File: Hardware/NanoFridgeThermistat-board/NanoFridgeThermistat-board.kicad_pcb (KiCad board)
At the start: 2 copper layers, 80.5 x 72 mm, 36 parts, among them J1 Connector_Thermistor, J2 Main_Connector, J3 CompressorMotor_Connector, J4 I2C_Conn, SW1 SW_Push, SW2 SW_Push, T1 CST1, U1 MOC3042M, U2 TL072

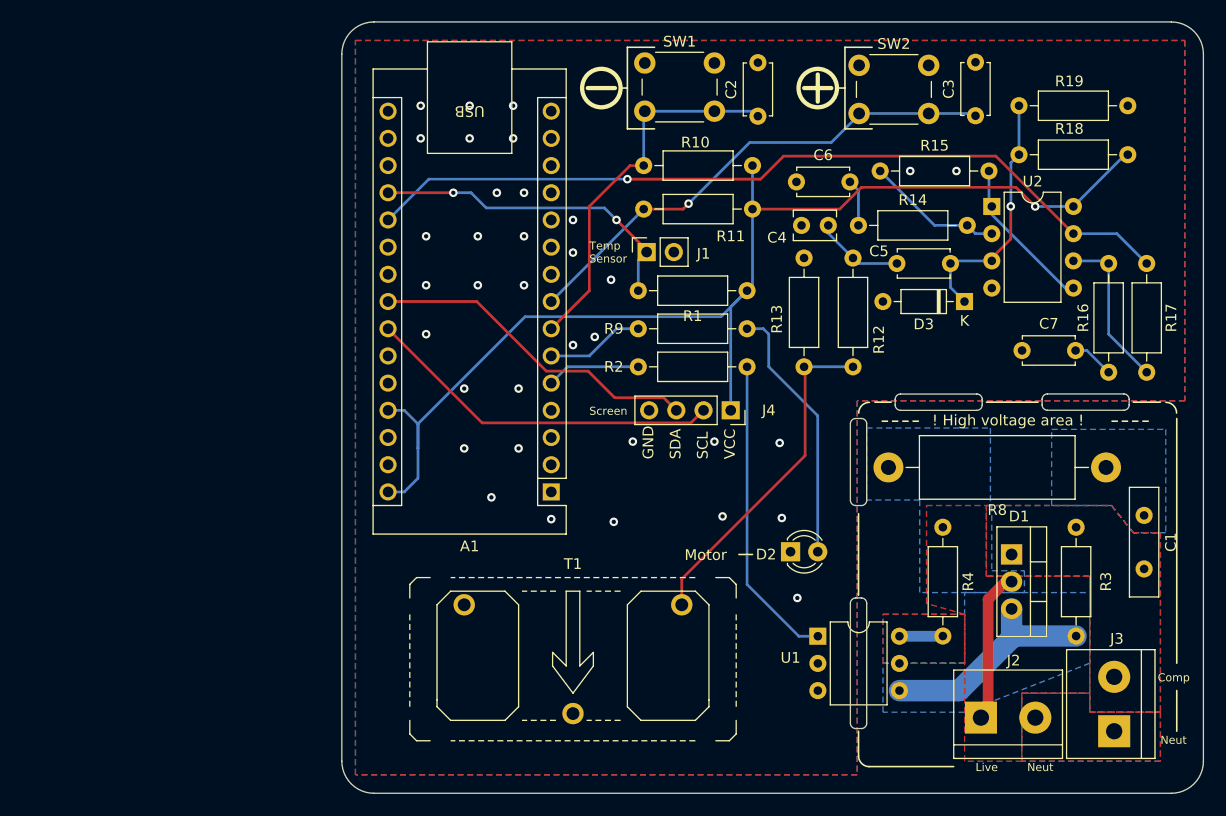
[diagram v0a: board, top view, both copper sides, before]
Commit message: Fixed last issues with DRC on PCB router
Signed-off-by: bebenlebricolo <benoittarrade@hotmail.fr>
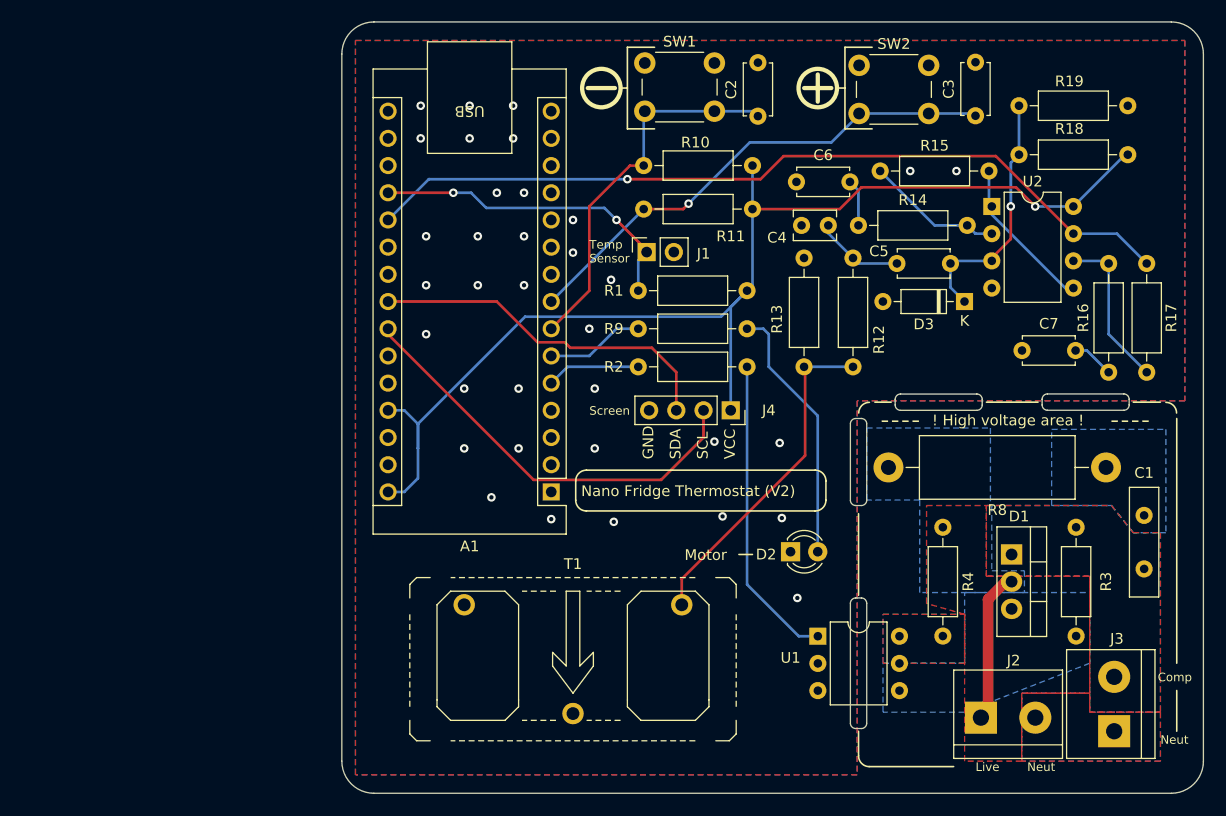
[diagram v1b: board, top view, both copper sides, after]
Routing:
- net /Trigger: track 21.3 -> 0.00 mm
- net SCL: track 33.6 -> 39.8 mm
- net /TriacDriverAC1: track 4.06 -> 0.00 mm
- net SDA: track 31.1 -> 33.2 mm
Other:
- board text added: "Designed by bebenlebricolo (Benoît Tarrade) 05/02/2024 (dd/mm/yyyy) https://github.com/bebenlebricolo/NanoFridgeThermostat"
- board text added: "Licensed under CERN OHL V2"
- board text added: "Nano Fridge Thermostat (V2)"

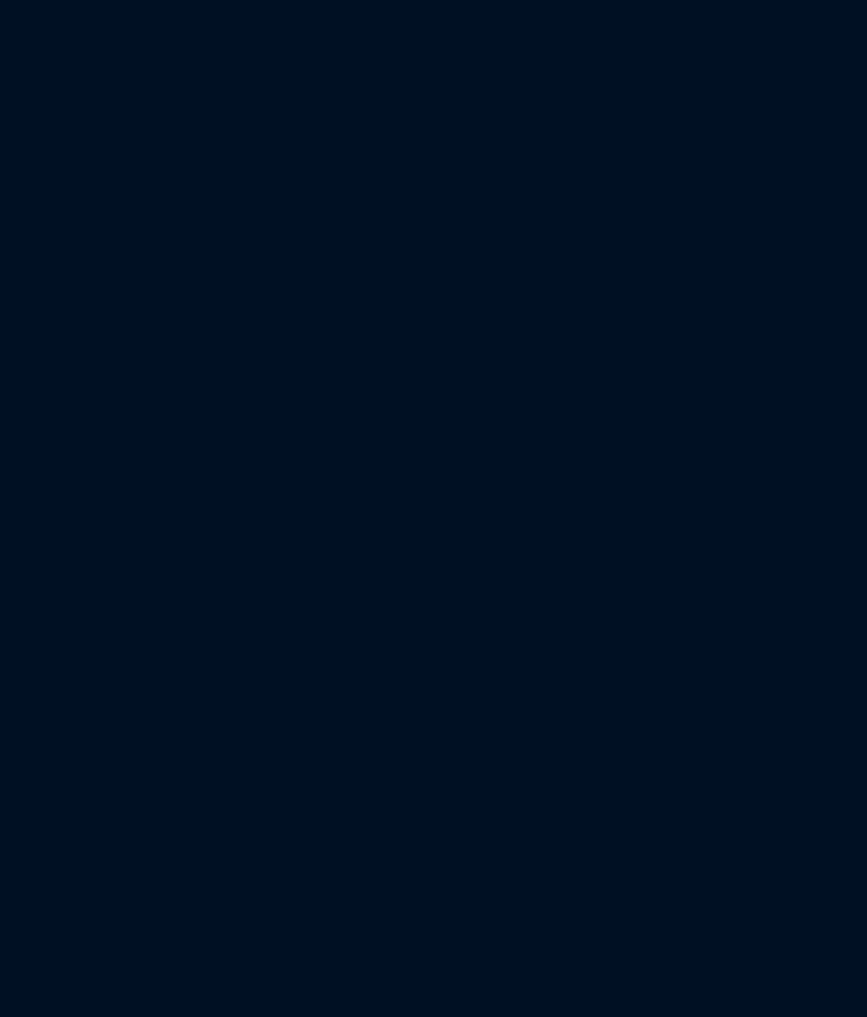
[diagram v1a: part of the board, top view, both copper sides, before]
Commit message: Adding mounting holes and test points
Signed-off-by: bebenlebricolo <benoittarrade@hotmail.fr>
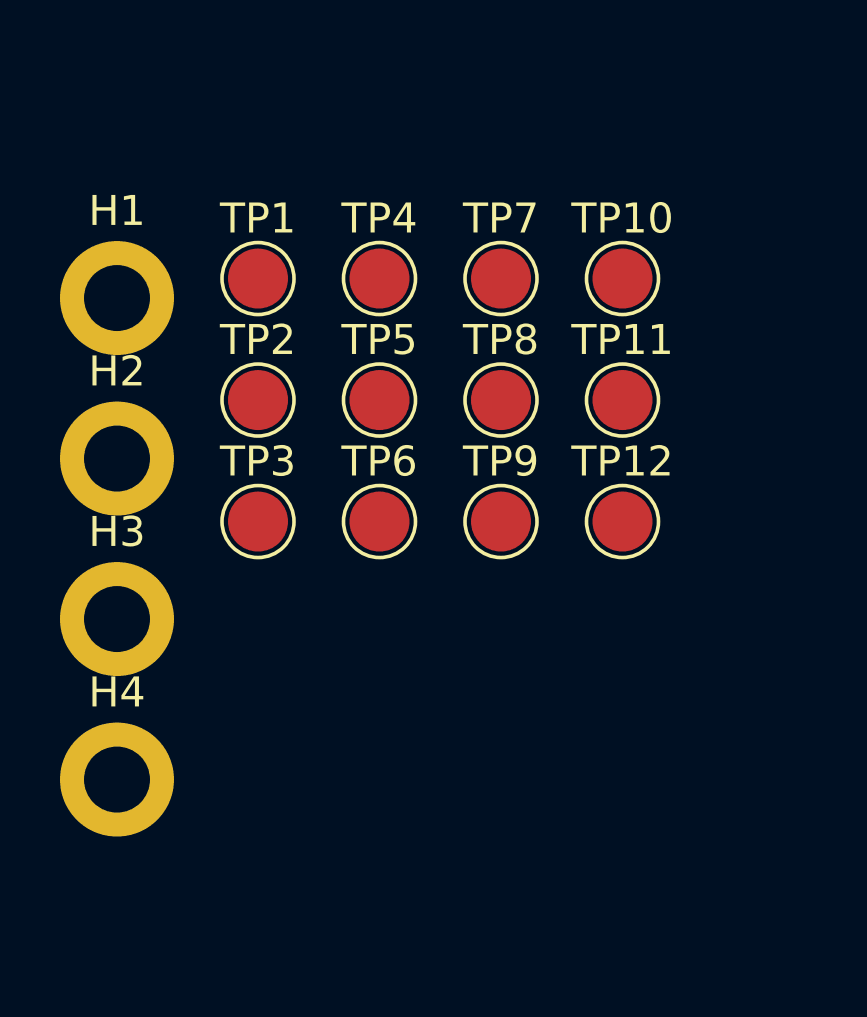
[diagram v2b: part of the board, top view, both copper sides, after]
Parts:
- added H1: MountingHole_Pad, MountingHole:MountingHole_2.2mm_M2_DIN965_Pad, F.Cu at (52.0, 68.0)
- added H2: MountingHole_Pad, MountingHole:MountingHole_2.2mm_M2_DIN965_Pad, F.Cu at (52.0, 73.3)
- added H3: MountingHole_Pad, MountingHole:MountingHole_2.2mm_M2_DIN965_Pad, F.Cu at (52.0, 78.7)
- added H4: MountingHole_Pad, MountingHole:MountingHole_2.2mm_M2_DIN965_Pad, F.Cu at (52.0, 84.0)
- added TP1: TestPoint, TestPoint:TestPoint_Pad_D2.0mm, F.Cu at (56.7, 67.3)
- added TP10: TestPoint, TestPoint:TestPoint_Pad_D2.0mm, F.Cu at (68.8, 67.3)
- added TP11: TestPoint, TestPoint:TestPoint_Pad_D2.0mm, F.Cu at (68.8, 71.4)
- added TP12: TestPoint, TestPoint:TestPoint_Pad_D2.0mm, F.Cu at (68.8, 75.4)
- added TP2: TestPoint, TestPoint:TestPoint_Pad_D2.0mm, F.Cu at (56.7, 71.4)
- added TP3: TestPoint, TestPoint:TestPoint_Pad_D2.0mm, F.Cu at (56.7, 75.4)
- added TP4: TestPoint, TestPoint:TestPoint_Pad_D2.0mm, F.Cu at (60.7, 67.3)
- added TP5: TestPoint, TestPoint:TestPoint_Pad_D2.0mm, F.Cu at (60.7, 71.4)
- added TP6: TestPoint, TestPoint:TestPoint_Pad_D2.0mm, F.Cu at (60.7, 75.4)
- added TP7: TestPoint, TestPoint:TestPoint_Pad_D2.0mm, F.Cu at (64.8, 67.3)
- added TP8: TestPoint, TestPoint:TestPoint_Pad_D2.0mm, F.Cu at (64.8, 71.4)
- added TP9: TestPoint, TestPoint:TestPoint_Pad_D2.0mm, F.Cu at (64.8, 75.4)

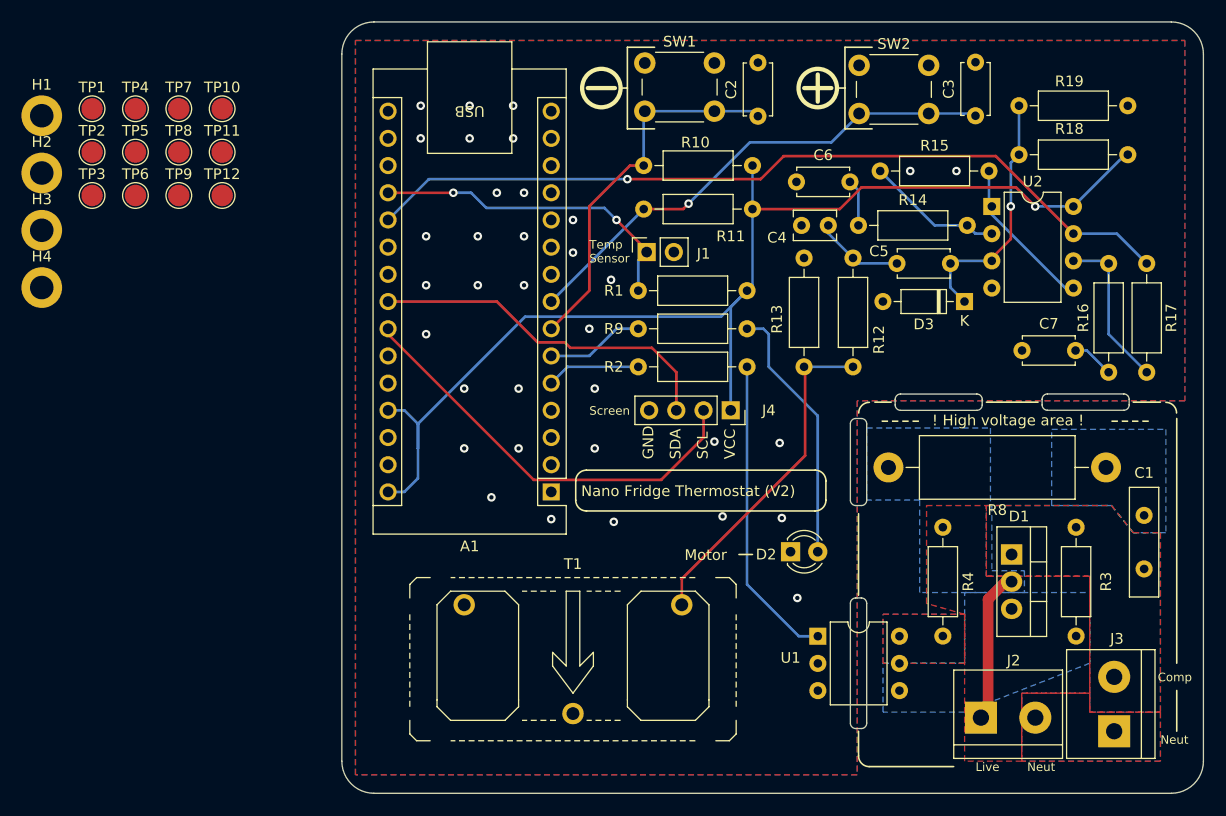
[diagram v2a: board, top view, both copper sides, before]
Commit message: Finalized board with testing points and mouse bites to detach AC board
Signed-off-by: bebenlebricolo <benoittarrade@hotmail.fr>
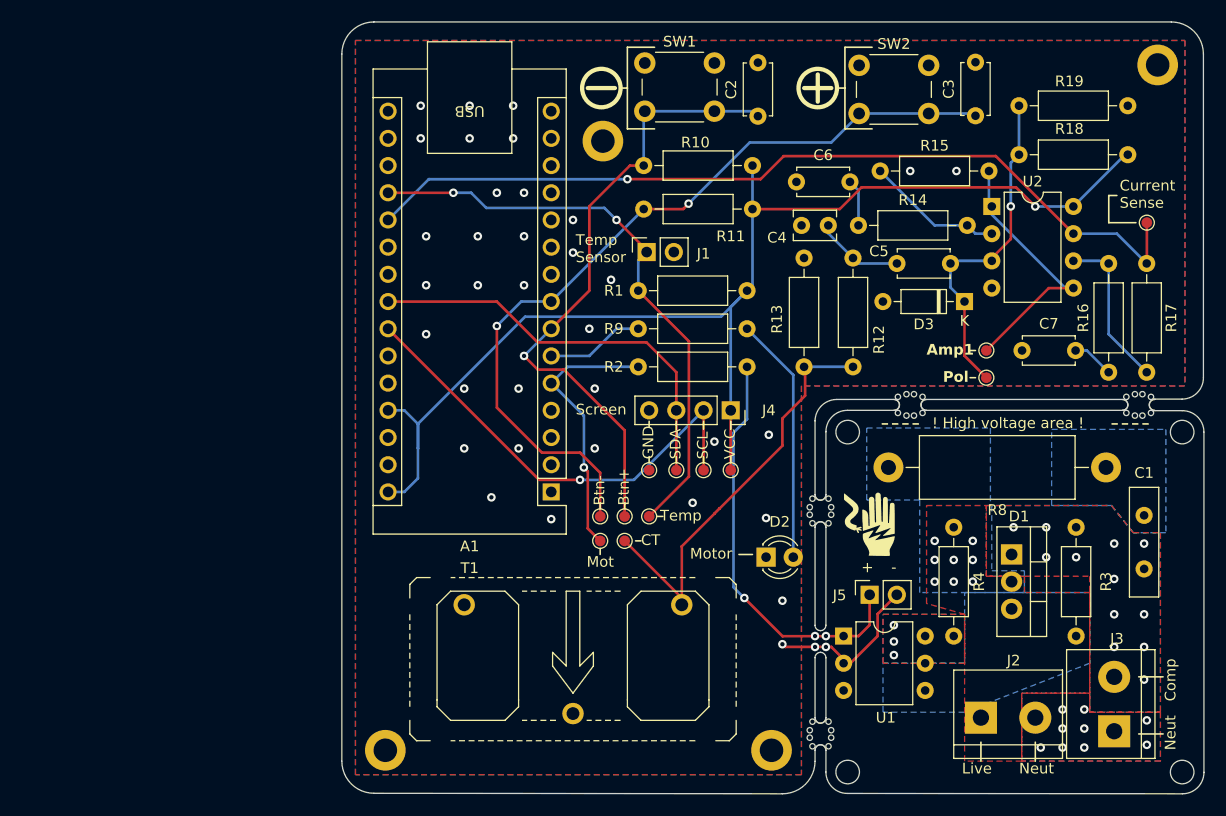
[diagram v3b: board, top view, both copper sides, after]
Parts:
- removed TP2: TestPoint, TestPoint:TestPoint_Pad_D2.0mm
- added G***: LOGO, LOGO, F.Cu at (129.3, 106.2)
- added G***: LOGO, LOGO, B.Cu at (131.1, 106.4)
- added H5: MountingHole, MountingHole:MountingHole_2.2mm_M2_ISO7380, F.Cu at (158.5, 97.5)
- added H6: MountingHole, MountingHole:MountingHole_2.2mm_M2_ISO7380, F.Cu at (127.3, 97.5)
- added H7: MountingHole, MountingHole:MountingHole_2.2mm_M2_ISO7380, F.Cu at (127.3, 129.3)
- added H8: MountingHole, MountingHole:MountingHole_2.2mm_M2_ISO7380, F.Cu at (158.5, 129.3)
- added J5: Connector_Thermistor, Connector_PinSocket_2.54mm:PinSocket_1x02_P2.54mm_Vertical, F.Cu at (129.3, 112.7)
- added TP13: TestPoint, TestPoint:TestPoint_Pad_D1.0mm, F.Cu at (108.7, 101.1)
- added mouse-bite-1mm-slot: VAL**, Panelization:mouse-bite-1mm-slot, F.Cu at (133.1, 95.0)
- added mouse-bite-1mm-slot: VAL**, Panelization:mouse-bite-1mm-slot, F.Cu at (154.4, 95.0)
- added mouse-bite-1mm-slot: VAL**, Panelization:mouse-bite-1mm-slot, F.Cu at (124.7, 104.9)
- added mouse-bite-1mm-slot: VAL**, Panelization:mouse-bite-1mm-slot, F.Cu at (124.7, 125.7)
- TP1, TP10, TP11, TP12, TP3, TP4, TP5, TP6, TP7, TP8, TP9: footprint TestPoint:TestPoint_Pad_D2.0mm -> TestPoint:TestPoint_Pad_D1.0mm
- moved H3 105.4 mm to (156.2, 63.2)
- moved TP7 91.0 mm to (155.2, 78.0)
- moved TP3 85.2 mm to (140.2, 92.5)
- moved TP6 80.8 mm to (140.2, 89.9)
- moved H4 80.7 mm to (120.1, 127.3)
- moved H1 67.4 mm to (84.1, 127.3)
- moved TP1 62.3 mm to (104.1, 107.7)
- moved TP4 59.5 mm to (106.4, 105.4)
- moved TP9 57.6 mm to (116.3, 101.1)
- moved TP10 56.2 mm to (113.8, 101.1)
- moved TP8 55.2 mm to (106.4, 107.7)
- moved TP5 55.2 mm to (104.1, 105.4)
- moved H2 52.5 mm to (104.4, 70.4)
- moved TP11 51.8 mm to (111.3, 101.1)
- moved TP12 49.9 mm to (108.7, 105.4)
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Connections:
- net Net-(R2-Pad2) renamed /TriacDriverEnable
- net Net-(T1-A) renamed /CTSense
- net Net-(U2B-+) renamed /Amp1
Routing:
- net -Button: track 47.1 -> 76.9 mm, vias 1 -> 2
- net Temp: track 30.5 -> 55.1 mm
- net +Button: track 35.4 -> 59.4 mm, vias 0 -> 1
- net MotorOut: track 8.76 -> 25.4 mm, vias 0 -> 1
- net GND: track 0.00 -> 15.5 mm, vias 35 -> 37
- net Main_HOT: track 14.0 -> 0.00 mm, vias 0 -> 8
- net /Amp1: track 14.6 -> 25.2 mm
- net /TriacDriverEnable: track 28.9 -> 39.0 mm, vias 0 -> 3
- net /CTSense: track 31.6 -> 39.8 mm
- net Polarisation: track 23.6 -> 31.6 mm
- net Vcc: track 112.8 -> 118.3 mm
- net SDA: track 33.2 -> 38.8 mm
- net SCL: track 39.8 -> 43.7 mm, vias 0 -> 1
- net CurrentSense: track 77.5 -> 81.3 mm
- net Net-(D2-A): track 24.5 -> 23.1 mm
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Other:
- board size 80.5 x 72 mm -> 80.5 x 72.1 mm
- board text added: "+"
- board text added: "-"
- board text added: "Amp1"
- board text added: "Btn+"
- board text added: "Btn-"
- board text added: "CT"
- board text added: "Current Sense"
- board text added: "Mot"
- board text added: "Nano Fridge Thermostat (V2) Daughter board"
- board text added: "Pol"
- board text added: "Temp"
